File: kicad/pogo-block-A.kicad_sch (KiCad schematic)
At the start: 9 parts, among them J1 L_IN, J2 R_IN, U1 OPA1612

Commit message: kicad: vendor BAT54S SOT-23 footprint + structural schematic verifier
Resolve the two items flagged in the block-A slice:

- BAT54S footprint: add kicad/footprints/Package_TO_SOT_SMD.pretty/SOT-23,
  bind it in the registry (was footprint: null), regen fp-lib-table + BOM.
  D1/D2 now resolve to POGO_Package_TO_SOT_SMD:SOT-23; all block-A parts
  have vendored footprints.
- Replace the weak paren-count check with an independent structural verifier:
  re-parses the emitted .kicad_sch as s-expr, re-derives each pin's connection
  point from lib_symbols geometry, and confirms every global label lands on a
  pin and every pin is labeled or an intended no_connect. Catches malformed
  s-expr, dangling lib_ids, and sym_*()/*_pins() geometry drift — the
  'would it connect in KiCad?' check without KiCad. Wired into --check.
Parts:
- D1, D2: footprint (none) -> POGO_Package_TO_SOT_SMD:SOT-23
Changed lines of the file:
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@@
   (property "Value" "BAT54S" (at 88.000 79.500 0)
     (effects (font (size 1.016 1.016)) (justify left) (hide yes)))
+  (property "Footprint" "POGO_Package_TO_SOT_SMD:SOT-23" (at 85.000 80.000 0)
+    (effects (font (size 1.016 1.016)) (hide yes)))
 )
 (symbol
@@
   (property "Value" "BAT54S" (at 133.000 79.500 0)
     (effects (font (size 1.016 1.016)) (justify left) (hide yes)))
+  (property "Footprint" "POGO_Package_TO_SOT_SMD:SOT-23" (at 130.000 80.000 0)
+    (effects (font (size 1.016 1.016)) (hide yes)))
 )
 (symbol

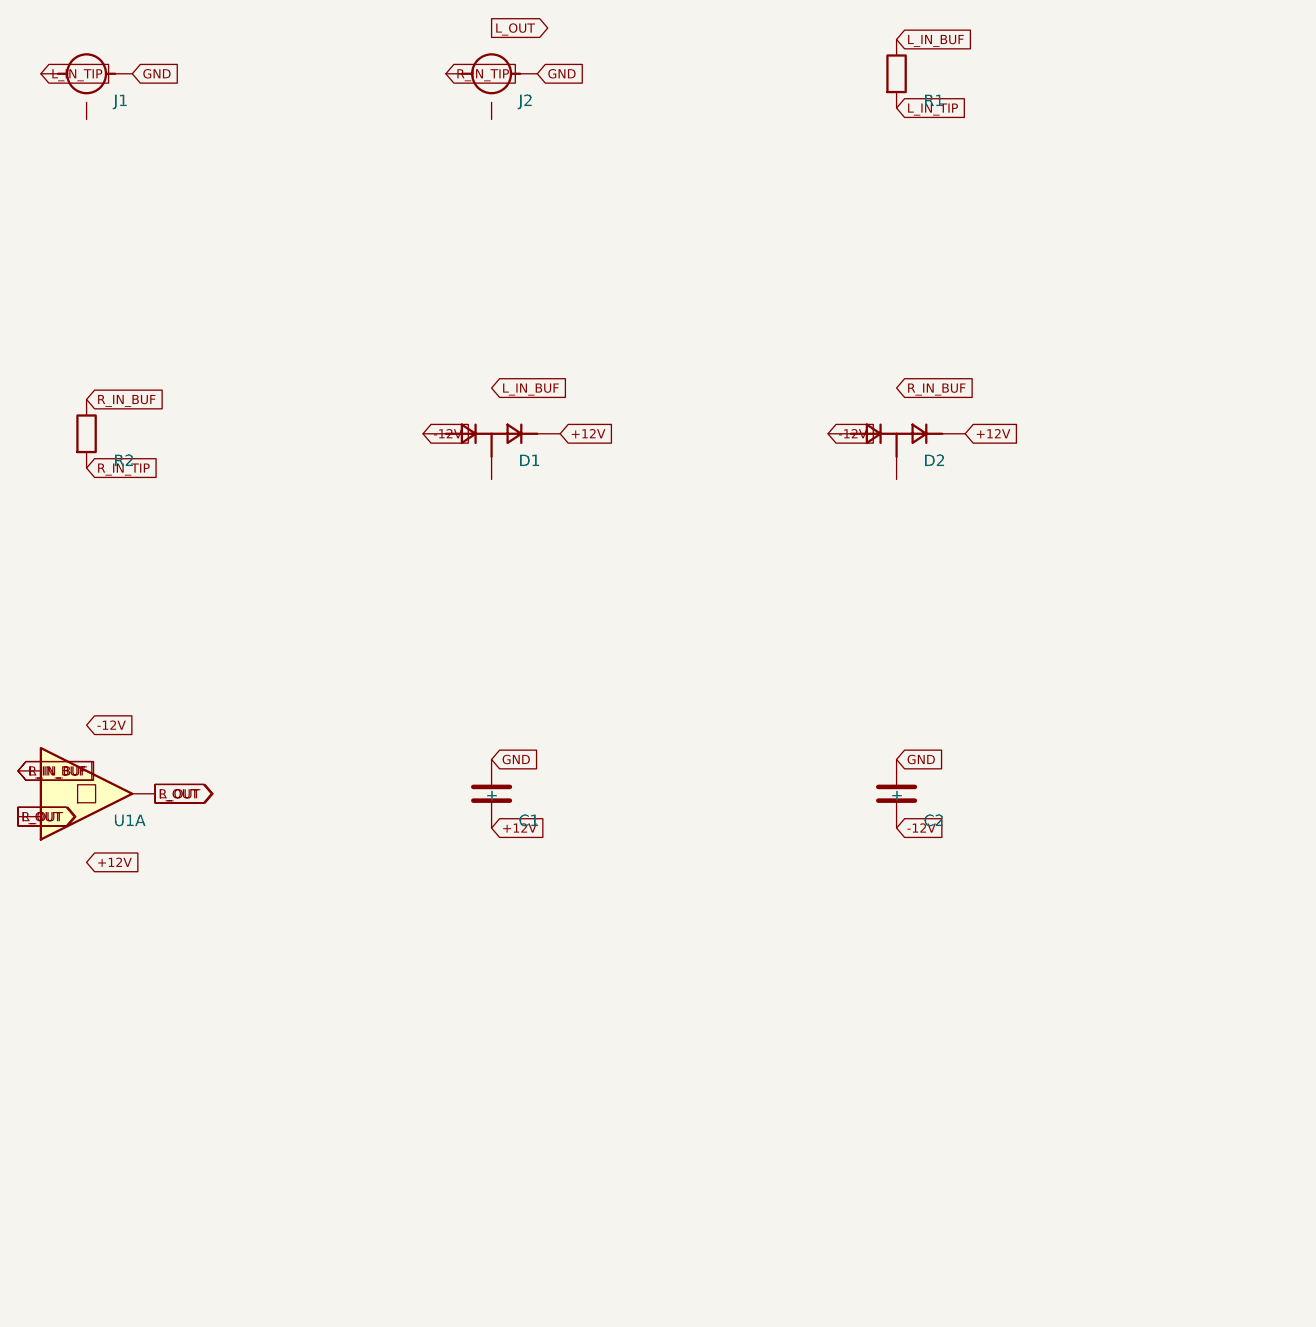
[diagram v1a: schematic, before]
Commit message: kicad: block-8 LP2 + fix multi-unit op-amp placement bug (7 of 10)
block-8 (LP2): OTA-C SVF mirroring LP1 minus tilt (single shared expo); Q VCA via
the shared-q sheet cell B (U9/U10); added LP2's own IRES_AMP (U65, was missing from
the BOM) + full SVF expansion (R_LIN, expo network, Q V->I, buffer pulldowns,
decoupling). 51 parts / 36 nets; LP2 boundary nets match shared-q byte-for-byte.
shared-q gains the LP2 cell-B Iabc bypass caps (C84/C85).

GENERATOR CORRECTNESS FIX (exposed by block-8's spare op-amp half): dual op-amps
were placed as a single instance while pins from BOTH halves were connected at the
lib_symbol's overlapping origin -> unit-A and unit-B pins landed on the same canvas
point, shorting the two halves. This was latent in EVERY dual-op-amp block (A,B,1,2,
4,5). Fix:
- place each gate unit (A/B/power) as its own instance at distinct offsets
  (MULTI_UNIT + opamp_unit_pins);
- make structural_check unit-aware (per-sub-symbol unit pins);
- add a short detector: 2+ distinct nets whose labels coincide at one point now fail.
All blocks regenerated and re-verified clean (the detector finds no shorts).

STATUS+plan: 7/10 blocks. All gates green.
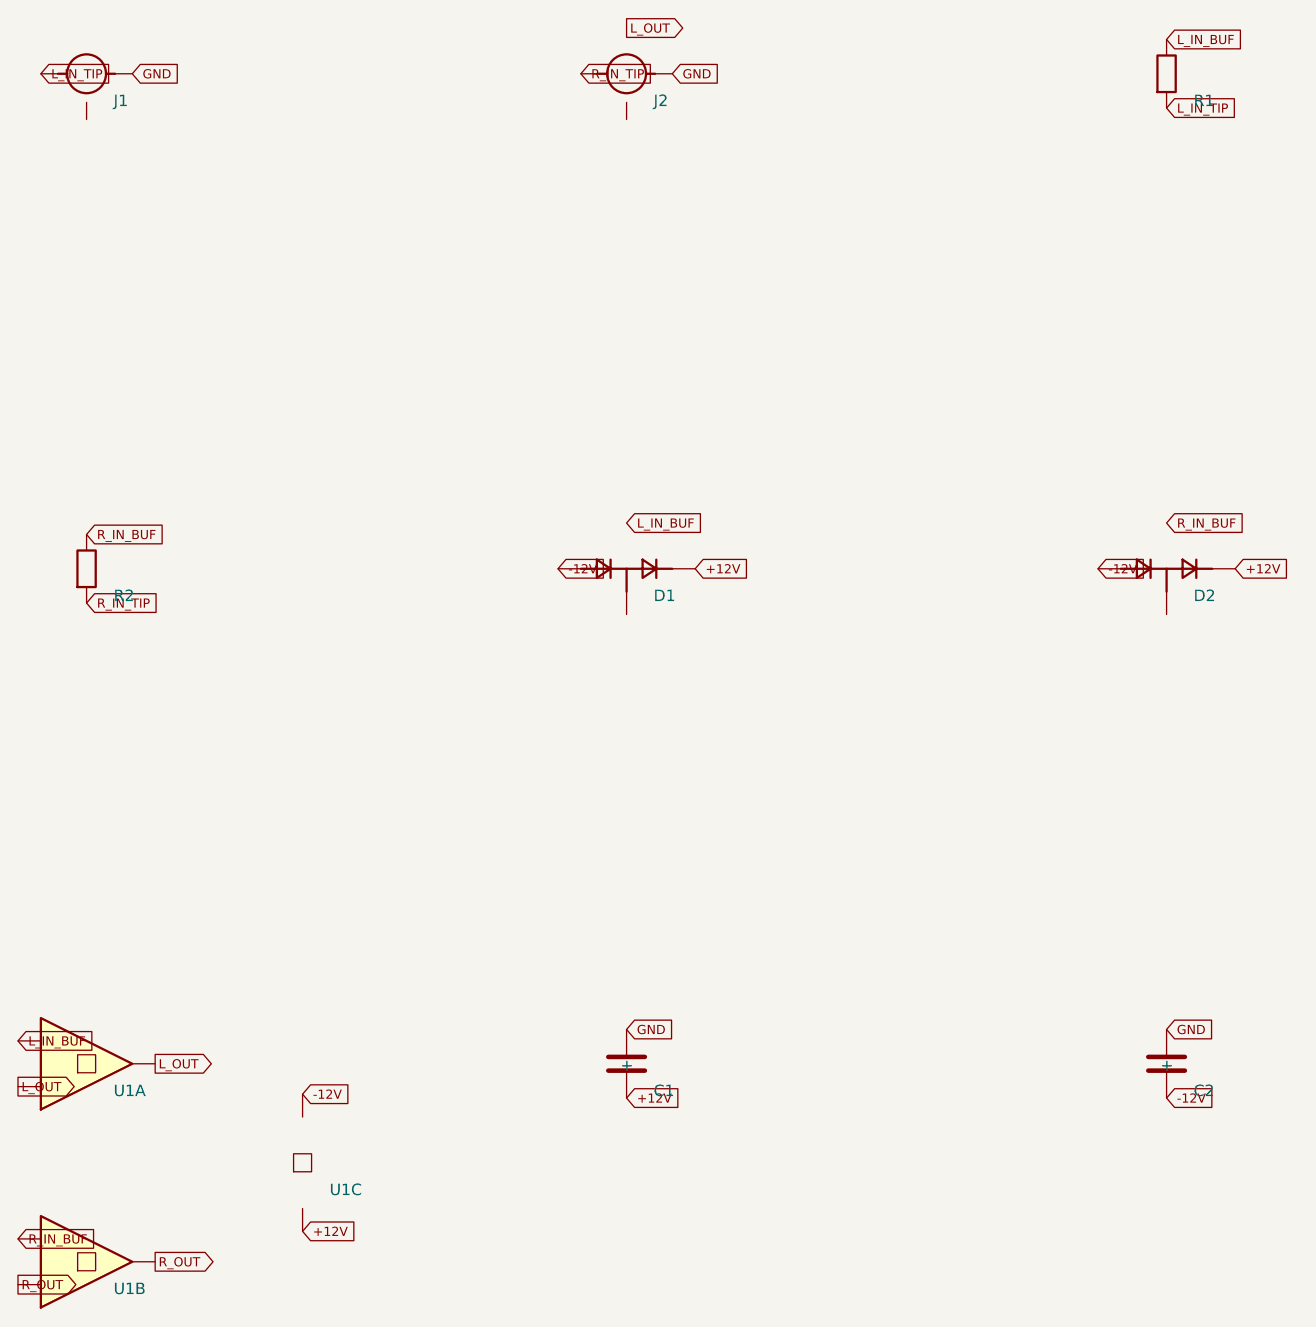
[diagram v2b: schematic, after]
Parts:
- added C1, C2: 100nF, symbol Device:C
- U1: renamed from C2; value 100nF -> OPA1612; symbol Device:C -> Amplifier_Operational:OPA1612
- U1: renamed from C1; value 100nF -> OPA1612; symbol Device:C -> Amplifier_Operational:OPA1612
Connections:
- net +12V: now also U1.4 (V-), C1.2; no longer U1.2
- net -12V: now also U1.8 (V+), C2.2; no longer U1.2
- net GND: now also C1.1 (+), C2.1 (+); no longer U1.1 (+), U1.1 (+)
- net L_IN_BUF: no longer R2.1
- new net R_IN_BUF: R2.1, U1.6 (In-)
- new net R_OUT: U1.5 (In+), U1.7 (Out)
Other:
- moved on the sheet: D1, D2, J2, R1, R2, U1A
